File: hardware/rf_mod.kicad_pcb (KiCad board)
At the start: 4 copper layers, 100 x 100 mm, 168 parts, among them J1001 SMA, J1002 SMA, J1003 SMA, J1004 Pmod, J101 SMA, J102 SMA, J103 SMA, J1201 SMA, J1202 SMA, J1301 SMA, J1302 SMA, J1303 SMA, J201 SMA, J202 SMA, J401 SMA, J402 SMA, J501 SMA, J502 SMA, J701 SMA, J702 SMA, J703 SMA, J801 SMA, J802 SMA, J803 SMA, J901 USB-C, J902 SMA, Q1001 AO3401A, Q1201 AO3401A, Q1301 AO3401A, Q501 AO3401A, Q701 AO3401A, Q801 AO3401A, SW1001 ON, SW1201 ON, SW1301 ON, SW501 ON, SW701 ON, SW801 ON, U1001 3.3V, U1002 MAX2871, U101 ADEX-10L+, U1201 GALI-84+, U1301 TRF3722, U1302 3.3V, U501 QPL9547, U701 3.3V, U702 ADL5350, U801 3.3V, U802 ADL5350, U901 MT3608, U902 3.3V, U903 74LVC1G17, X901 25 MHz

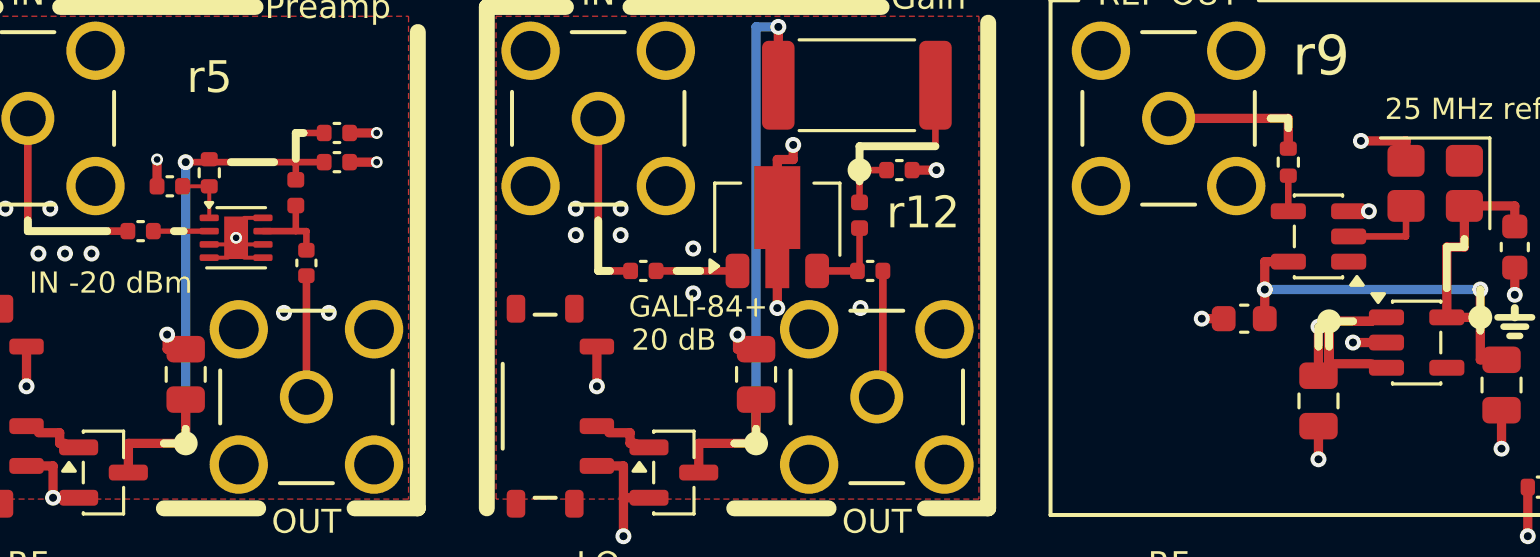
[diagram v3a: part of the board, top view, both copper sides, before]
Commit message: Pre-order checks from CLAUDE_PCB.md's new lessons (Prompt 21): the KF301 terminals turned for their wire openings (CPL +180, body 3.7 / 4.0, a wire-face check), four oversold parts swapped (27R, 6.8k, 220n, OPA847IDBVT at its own +180), fourteen vias moved out of SMD pads (check_layout.py gates it and RF detours), 200-250 mW terminations, assembly drawings from Fab and silk fitted to Letter (fit_pdf.py from CostasLink), the stock gate on JLCPCB's free count, electrolytics in the rotation check, the RF gates surveyed (rf_extract.py, rf_survey.py) and written into the DOA lists; all nine boards rebuilt: ERC 0, DRC 0, every check
Co-Authored-By: Claude Opus 5.5 <noreply@anthropic.com>
Claude-Session: https://claude.ai/code/session_01RKeoKvFFzjk3cEBLCXXHnB
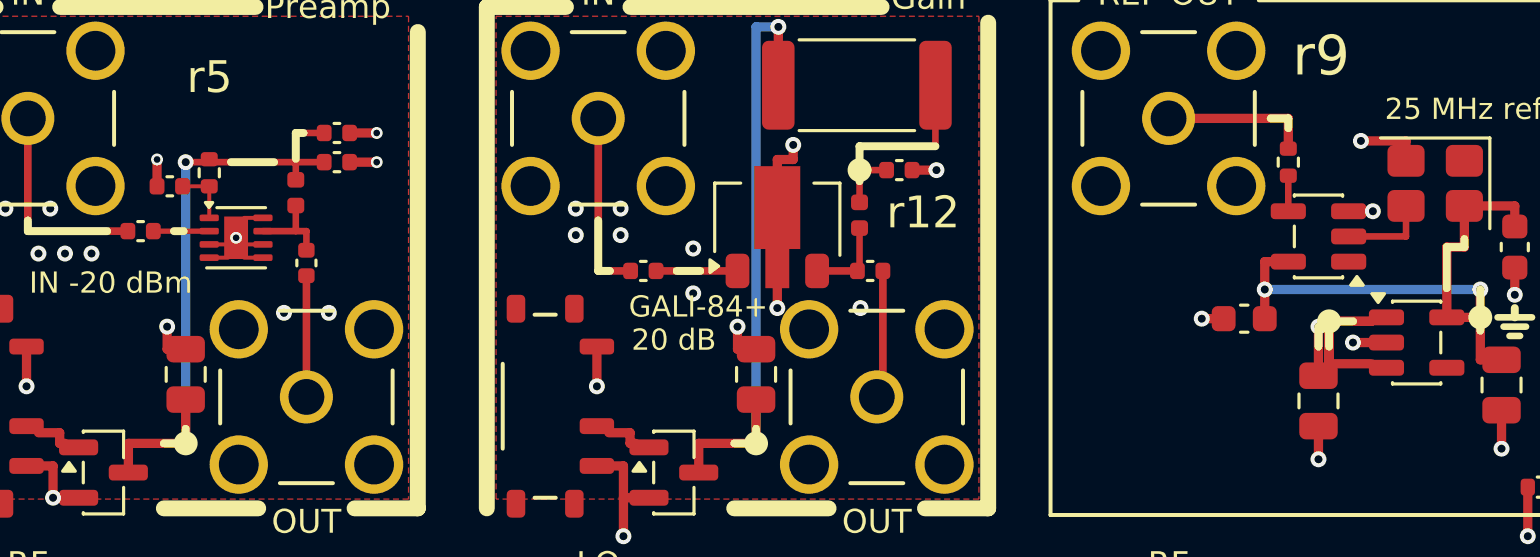
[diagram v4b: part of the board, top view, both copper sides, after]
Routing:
- net GND: track 154.7 -> 155.5 mm
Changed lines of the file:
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@@
 	)
 	(segment
-		(start 39.25 42.7)
-		(end 39.25 42.15)
-		(width 0.35)
-		(layer "F.Cu")
-		(net "GND")
-	)
-	(segment
 		(start 60.75 17.176)
 		(end 60.75 16.149999)
@@
 	)
 	(segment
-		(start 17.75 42.7)
-		(end 17.75 42.15)
+		(start 21.25 82.75)
+		(end 20.65 82.15)
 		(width 0.35)
 		(layer "F.Cu")
@@
 	)
 	(segment
-		(start 21.25 82.75)
-		(end 20.65 82.15)
+		(start 62.2875 37.5)
+		(end 63.2 37.5)
 		(width 0.35)
 		(layer "F.Cu")
@@
 	)
 	(segment
+		(start 17.75 42.7)
+		(end 17.75 41.85)
+		(width 0.35)
+		(layer "F.Cu")
+		(net "GND")
+	)
+	(segment
 		(start 64.15 82.7)
 		(end 65.349999 81.5)
@@
 	)
 	(segment
+		(start 39.25 42.7)
+		(end 39.25 41.85)
+		(width 0.35)
+		(layer "F.Cu")
+		(net "GND")
+	)
+	(segment
 		(start 39.95 42.7)
 		(end 39.25 42.7)
@@
 	)
 	(segment
-		(start 62.2875 37.5)
-		(end 63.05 37.5)
-		(width 0.35)
-		(layer "F.Cu")
-		(net "GND")
-	)
-	(segment
 		(start 20 76.975)
 		(end 20 76.15)
@@
 	)
 	(via
-		(at 17.75 42.15)
-		(size 0.6)
-		(drill 0.3)
-		(layers "F.Cu" "B.Cu")
-		(tenting
-			(front yes)
-			(back yes)
-		)
-		(net "GND")
-	)
-	(via
 		(at 80.23 82.105)
 		(size 0.6)
@@
 	)
 	(via
-		(at 63.05 37.5)
-		(size 0.6)
-		(drill 0.3)
-		(layers "F.Cu" "B.Cu")
-		(tenting
-			(front yes)
-			(back yes)
-		)
-		(net "GND")
-	)
-	(via
 		(at 15.405 90.43)
 		(size 0.6)
@@
 	)
 	(via
-		(at 39.25 42.15)
-		(size 0.6)
-		(drill 0.3)
-		(layers "F.Cu" "B.Cu")
-		(tenting
-			(front yes)
-			(back yes)
-		)
-		(net "GND")
-	)
-	(via
 		(at 28.93 60.495)
 		(size 0.6)
@@
 	)
 	(via
+		(at 63.2 37.5)
+		(size 0.6)
+		(drill 0.3)
+		(layers "F.Cu" "B.Cu")
+		(tenting
+			(front yes)
+			(back yes)
+		)
+		(net "GND")
+	)
+	(via
 		(at 14.9 59.905)
 		(size 0.6)
@@
 	)
 	(via
+		(at 17.75 41.85)
+		(size 0.6)
+		(drill 0.3)
+		(layers "F.Cu" "B.Cu")
+		(tenting
+			(front yes)
+			(back yes)
+		)
+		(net "GND")
+	)
+	(via
 		(at 75.45 87.1)
 		(size 0.6)
@@
 		(size 0.6)
 		(drill 0.3)
+		(layers "F.Cu" "B.Cu")
+		(tenting
+			(front yes)
+			(back yes)
+		)
+		(net "GND")
+	)
+	(via
+		(at 39.25 41.85)
+		(size 0.6)
+		(drill 0.3)
